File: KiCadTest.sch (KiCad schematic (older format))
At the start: 6 parts, among them J1 Conn_02x25_Odd_Even, U1 25LCxxx, U2 74HC4051, U3 25LCxxx

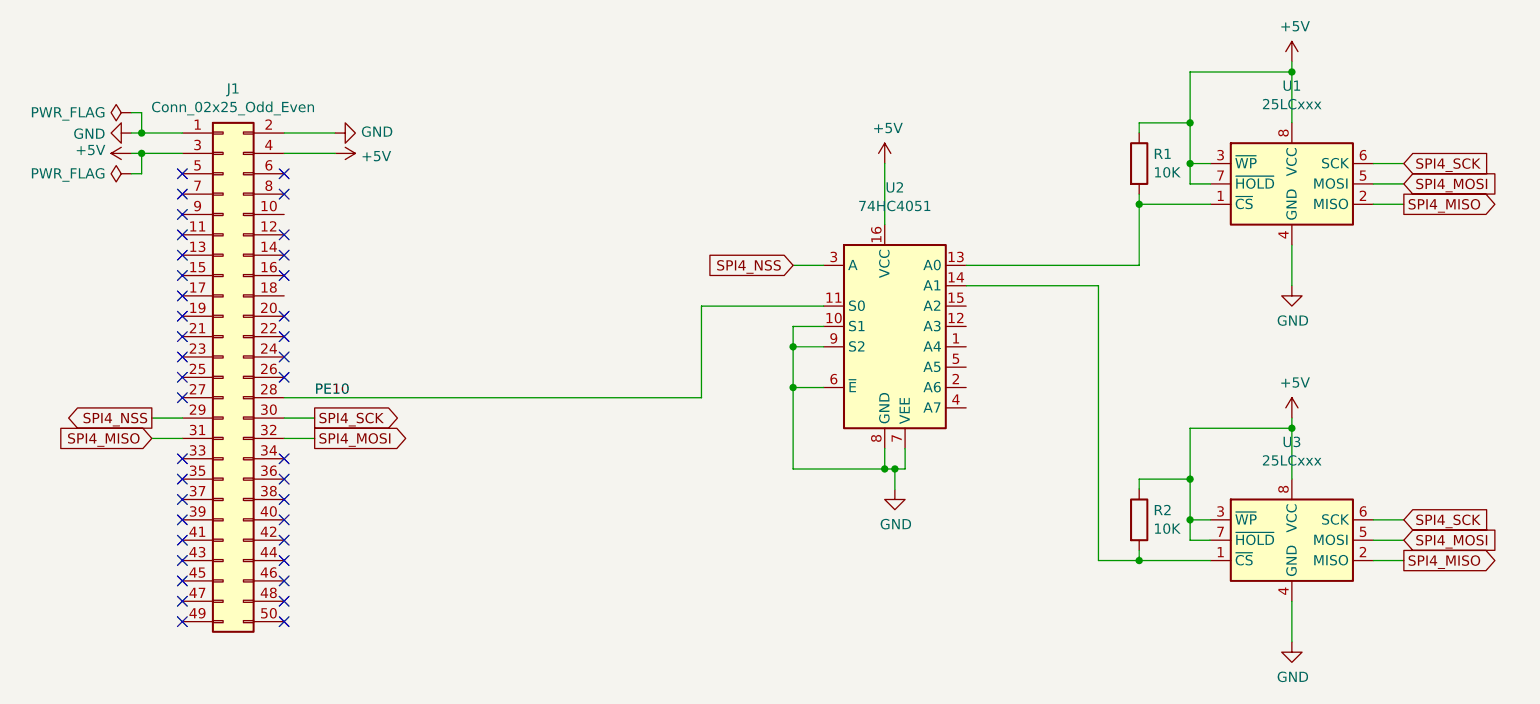
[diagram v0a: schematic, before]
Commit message: Reroute some PCB tracks and switch 5V for VDD
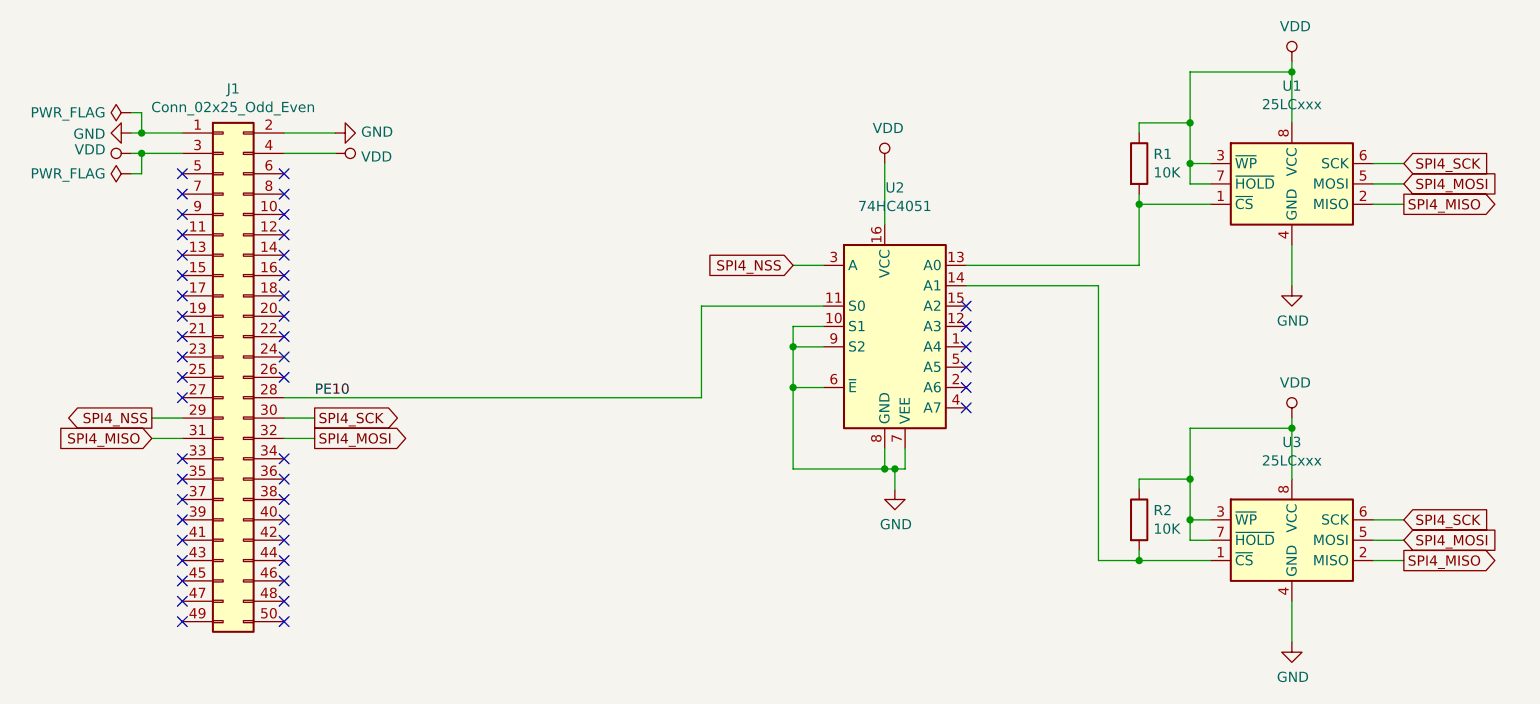
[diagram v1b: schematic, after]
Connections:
- net +5V renamed VDD
- no-connect marks 39 -> 47
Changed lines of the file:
@@
 Wire Wire Line
 	8300 3100 8300 3300
-$Comp
-L power:+5V #PWR0104
-U 1 1 5F4BAAE7
-P 8300 2200
-F 0 "#PWR0104" H 8300 2050 50  0001 C CNN
-F 1 "+5V" H 8315 2373 50  0000 C CNN
-F 2 "" H 8300 2200 50  0001 C CNN
-F 3 "" H 8300 2200 50  0001 C CNN
-	1    8300 2200
-	1    0    0    -1
-$EndComp
 Wire Wire Line
 	8300 2200 8300 2250
 Wire Wire Line
 	3350 2650 3600 2650
-$Comp
-L power:+5V #PWR0105
-U 1 1 5F4BC1A5
-P 3600 2650
-F 0 "#PWR0105" H 3600 2500 50  0001 C CNN
-F 1 "+5V" V 3615 2778 50  0000 L CNN
-F 2 "" H 3600 2650 50  0001 C CNN
-F 3 "" H 3600 2650 50  0001 C CNN
-	1    3600 2650
-	0    1    1    0
-$EndComp
-$Comp
-L power:+5V #PWR0106
-U 1 1 5F4C0B41
-P 2600 2650
-F 0 "#PWR0106" H 2600 2500 50  0001 C CNN
-F 1 "+5V" V 2615 2778 50  0000 L CNN
-F 2 "" H 2600 2650 50  0001 C CNN
-F 3 "" H 2600 2650 50  0001 C CNN
-	1    2600 2650
-	0    -1   -1   0
-$EndComp
 Wire Wire Line
 	2600 2650 2650 2650
@@
 Wire Wire Line
 	8300 4850 8300 5050
-$Comp
-L power:+5V #PWR03
-U 1 1 5F4BFFBD
-P 8300 3950
-F 0 "#PWR03" H 8300 3800 50  0001 C CNN
-F 1 "+5V" H 8315 4123 50  0000 C CNN
-F 2 "" H 8300 3950 50  0001 C CNN
-F 3 "" H 8300 3950 50  0001 C CNN
-	1    8300 3950
-	1    0    0    -1
-$EndComp
 Wire Wire Line
 	8300 3950 8300 4000
@@
 	6400 4200 6350 4200
 Connection ~ 6350 4200
-$Comp
-L power:+5V #PWR01
-U 1 1 5F4C9CFF
-P 6300 2700
-F 0 "#PWR01" H 6300 2550 50  0001 C CNN
-F 1 "+5V" H 6315 2873 50  0000 C CNN
-F 2 "" H 6300 2700 50  0001 C CNN
-F 3 "" H 6300 2700 50  0001 C CNN
-	1    6300 2700
-	1    0    0    -1
-$EndComp
 Wire Wire Line
 	6300 2700 6300 3000
@@
 Wire Wire Line
 	5850 3200 6000 3200
+$Comp
+L power:VDD #PWR0104
+U 1 1 5F4BB763
+P 2600 2650
+F 0 "#PWR0104" H 2600 2500 50  0001 C CNN
+F 1 "VDD" V 2618 2777 50  0000 L CNN
+F 2 "" H 2600 2650 50  0001 C CNN
+F 3 "" H 2600 2650 50  0001 C CNN
+	1    2600 2650
+	0    -1   -1   0
+$EndComp
+$Comp
+L power:VDD #PWR0105
+U 1 1 5F4BED22
+P 3600 2650
+F 0 "#PWR0105" H 3600 2500 50  0001 C CNN
+F 1 "VDD" V 3617 2778 50  0000 L CNN
+F 2 "" H 3600 2650 50  0001 C CNN
+F 3 "" H 3600 2650 50  0001 C CNN
+	1    3600 2650
+	0    1    1    0
+$EndComp
+$Comp
+L power:VDD #PWR0106
+U 1 1 5F4BF582
+P 6300 2700
+F 0 "#PWR0106" H 6300 2550 50  0001 C CNN
+F 1 "VDD" H 6317 2873 50  0000 C CNN
+F 2 "" H 6300 2700 50  0001 C CNN
+F 3 "" H 6300 2700 50  0001 C CNN
+	1    6300 2700
+	1    0    0    -1
+$EndComp
+$Comp
+L power:VDD #PWR0107
+U 1 1 5F4BFAA5
+P 8300 2200
+F 0 "#PWR0107" H 8300 2050 50  0001 C CNN
+F 1 "VDD" H 8317 2373 50  0000 C CNN
+F 2 "" H 8300 2200 50  0001 C CNN
+F 3 "" H 8300 2200 50  0001 C CNN
+	1    8300 2200
+	1    0    0    -1
+$EndComp
+$Comp
+L power:VDD #PWR0108
+U 1 1 5F4BFF07
+P 8300 3950
+F 0 "#PWR0108" H 8300 3800 50  0001 C CNN
+F 1 "VDD" H 8317 4123 50  0000 C CNN
+F 2 "" H 8300 3950 50  0001 C CNN
+F 3 "" H 8300 3950 50  0001 C CNN
+	1    8300 3950
+	1    0    0    -1
+$EndComp
+NoConn ~ 6700 3400
+NoConn ~ 6700 3500
+NoConn ~ 6700 3600
+NoConn ~ 6700 3700
+NoConn ~ 6700 3800
+NoConn ~ 6700 3900
+NoConn ~ 3350 2950
+NoConn ~ 3350 3350
 $EndSCHEMATC
